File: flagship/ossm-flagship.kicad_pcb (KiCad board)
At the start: 6 copper layers, 58 x 58 mm, 0 parts

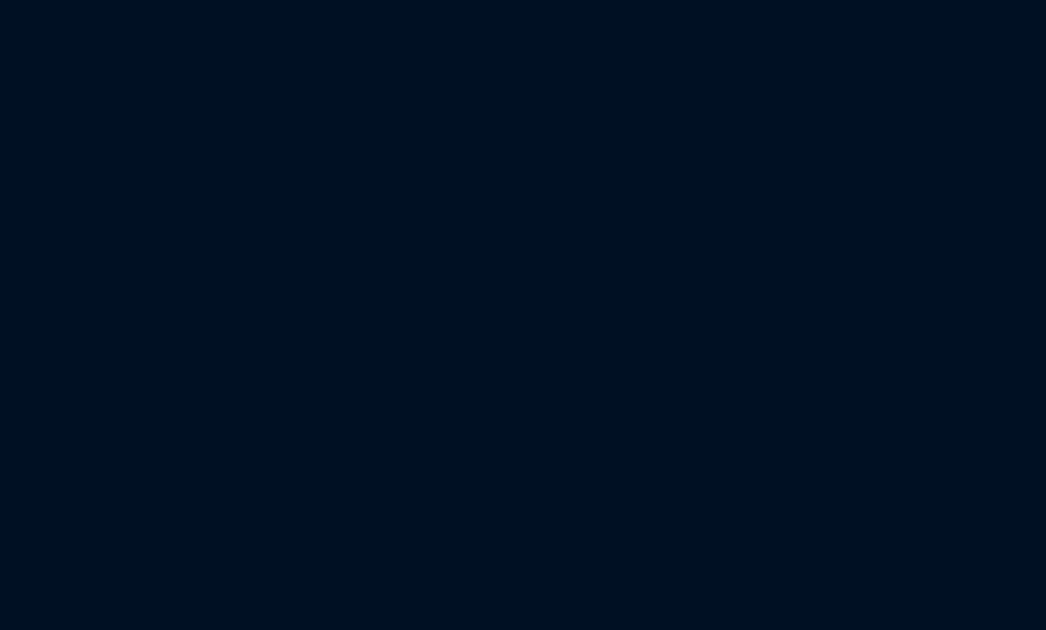
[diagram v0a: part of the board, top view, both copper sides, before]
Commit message: flagship: schematic skeleton across all seven sheets
Candidate ICs placed with cross-sheet nets as global labels and a design note per sheet
citing the record: LTC4364IS-2 input protection with INA228 Kelvin shunt and mirrored bulk;
TPS48111 back-to-back motor switch with pre-charge, MOTOR_EN pulldown, INA ALERT hardware
cut; TLV1805 + TLV431 self-acting regen clamp, 2x TO-263, external connector and
parallel/replace jumper; 3x TPS54560B bucks (12/5/3.3 V); Stamp-P4 with fixed pins only
(GPIO assignment follows layout, per ruling); THVD1450 RS485, 74AHCT125 quadrature, drive
status inputs; INA228, thermistor and fan headers. Connectors are generic placeholders.

SPEC.md: rulings for no RP2350 (P4 LP-core emits quadrature) and passive sizes.
Libraries normalized to ASCII (LCSC Chinese manufacturer names, en-dash pin name) after
they broke the MCP server's Windows-codepage reads.

ERC: 109 unconnected pins (detailing), 62 pin-type warnings (LCSC symbols ship
unspecified pin types), 13 one-sided labels (GPIO pending layout); 0 dangling.

Co-Authored-By: Claude Opus 5.5 (1M context) <noreply@anthropic.com>
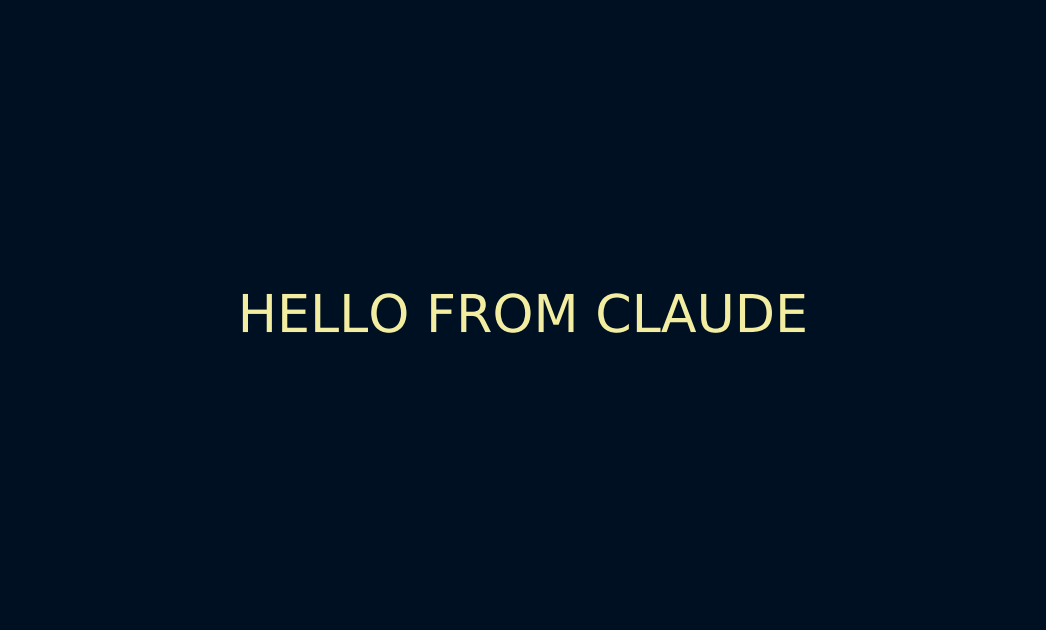
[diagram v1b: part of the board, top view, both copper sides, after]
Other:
- board text added: "HELLO FROM CLAUDE"
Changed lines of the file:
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@@
 		(layer "Edge.Cuts")
+	)
+	(gr_text "HELLO FROM CLAUDE"
+		(at 129 129 0)
+		(layer "F.SilkS")
+		(effects
+			(font
+				(size 1.27 1.27)
+			)
+		)
 	)
 	(zone
